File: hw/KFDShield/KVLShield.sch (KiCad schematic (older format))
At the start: 34 parts, among them J1 MR_Block, J2 OLED, J3 MR_Jack, P1 Power, P2 Analog, P3 Digital, P4 Digital, P5 CONN_01X01, P6 CONN_01X01, P7 CONN_01X01, P8 CONN_01X01, Q1 MMBT3904LT1G, Q2 MMBT3904LT1G, SW1 SW_Push, SW2 Up, SW3 Down, SW4 Enter

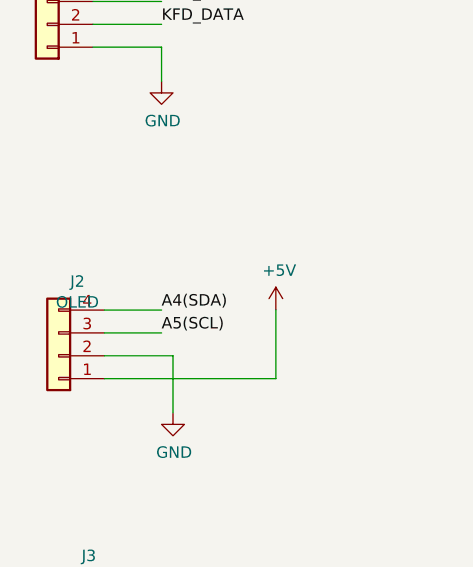
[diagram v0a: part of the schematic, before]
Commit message: recommended pcb updates
- got (almost) all traces on top layer
- increased trace widths
- moved around buttons to make trace routing cleaner
- added stitching vias to connect top/bottom ground pours
- moved gerbers to gerber directory, only exported necessary layers
- rearranged components for KFD signal lines for better routing

I think that's it
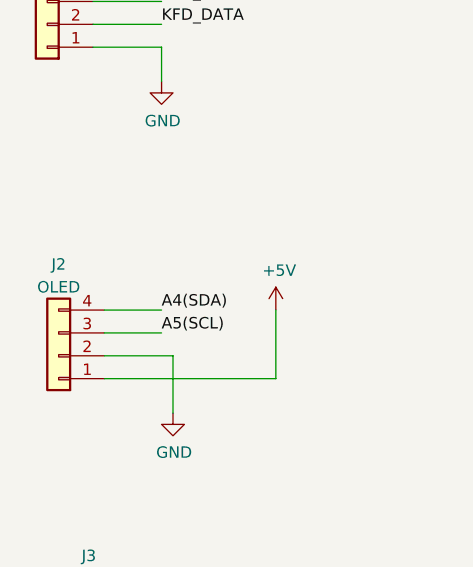
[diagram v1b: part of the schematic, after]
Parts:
- J2: footprint Connector_PinHeader_2.54mm:PinHeader_1x04_P2.54mm_Vertical -> Connector_PinSocket_2.54mm:PinSocket_1x04_P2.54mm_Vertical
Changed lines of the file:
@@
 U 1 1 61790991
 P 1000 4950
-F 0 "J2" H 918 4625 50  0000 C CNN
-F 1 "OLED" H 918 4716 50  0000 C CNN
-F 2 "Connector_PinHeader_2.54mm:PinHeader_1x04_P2.54mm_Vertical" H 1000 4950 50  0001 C CNN
+F 0 "J2" H 1000 4550 50  0000 C CNN
+F 1 "OLED" H 1000 4650 50  0000 C CNN
+F 2 "Connector_PinSocket_2.54mm:PinSocket_1x04_P2.54mm_Vertical" H 1000 4950 50  0001 C CNN
 F 3 "~" H 1000 4950 50  0001 C CNN
 	1    1000 4950

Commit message: beta hw rev sent to fab house
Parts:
- J3: footprint Connector_Audio:Jack_3.5mm_CUI_SJ-3523-SMT_Horizontal -> Connector_Audio:Jack_3.5mm_PJ320D_Horizontal; symbol Connector:AudioJack3 -> Connector:AudioJack4
- SW2, SW3, SW4: footprint Button_Switch_SMD:SW_SPST_FSMSM -> Button_Switch_SMD:SW_SPST_CK_RS282G05A3
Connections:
- net GND: now also J3.R2
- net KFD_SENSE: now also J3.R1; no longer J3.R
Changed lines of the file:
@@
 F 0 "SW2" V 3746 4202 50  0000 R CNN
 F 1 "Up" V 3655 4202 50  0000 R CNN
-F 2 "Button_Switch_SMD:SW_SPST_FSMSM" H 3700 4450 50  0001 C CNN
+F 2 "Button_Switch_SMD:SW_SPST_CK_RS282G05A3" H 3700 4450 50  0001 C CNN
 F 3 "~" H 3700 4450 50  0001 C CNN
 	1    3700 4250
@@
 F 0 "SW3" V 4696 4202 50  0000 R CNN
 F 1 "Down" V 4605 4202 50  0000 R CNN
-F 2 "Button_Switch_SMD:SW_SPST_FSMSM" H 4650 4450 50  0001 C CNN
+F 2 "Button_Switch_SMD:SW_SPST_CK_RS282G05A3" H 4650 4450 50  0001 C CNN
 F 3 "~" H 4650 4450 50  0001 C CNN
 	1    4650 4250
@@
 F 0 "SW4" V 5596 4202 50  0000 R CNN
 F 1 "Enter" V 5505 4202 50  0000 R CNN
-F 2 "Button_Switch_SMD:SW_SPST_FSMSM" H 5550 4450 50  0001 C CNN
+F 2 "Button_Switch_SMD:SW_SPST_CK_RS282G05A3" H 5550 4450 50  0001 C CNN
 F 3 "~" H 5550 4450 50  0001 C CNN
 	1    5550 4250
@@
 Connection ~ 6750 1500
 $Comp
-L Connector:AudioJack3 J3
+L Connector:AudioJack4 J3
 U 1 1 618A1DA3
 P 1150 6150
 F 0 "J3" H 1132 6475 50  0000 C CNN
 F 1 "MR_Jack" H 1132 6384 50  0000 C CNN
-F 2 "Connector_Audio:Jack_3.5mm_CUI_SJ-3523-SMT_Horizontal" H 1150 6150 50  0001 C CNN
+F 2 "Connector_Audio:Jack_3.5mm_PJ320D_Horizontal" H 1150 6150 50  0001 C CNN
 F 3 "~" H 1150 6150 50  0001 C CNN
 	1    1150 6150
 	1    0    0    -1
 $EndComp
+Text Label 1900 6350 0    50   ~ 0
+KFD_DATA
 Text Label 1900 6250 0    50   ~ 0
-KFD_DATA
-Text Label 1900 6150 0    50   ~ 0
 KFD_SENSE
 $Comp
@@
 	1350 6250 1900 6250
 Wire Wire Line
-	1350 6150 1900 6150
-Wire Wire Line
-	1350 6050 1550 6050
+	1350 6050 1450 6050
 Wire Wire Line
 	1550 6050 1550 6500
+Wire Wire Line
+	1350 6350 1900 6350
+Wire Wire Line
+	1350 6150 1450 6150
+Wire Wire Line
+	1450 6150 1450 6050
+Connection ~ 1450 6050
+Wire Wire Line
+	1450 6050 1550 6050
 $EndSCHEMATC
